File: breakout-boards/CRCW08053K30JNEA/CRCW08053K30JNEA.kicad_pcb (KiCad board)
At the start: 2 copper layers, 14 parts, among them J1 Conn_01x12, J2 Conn_01x12

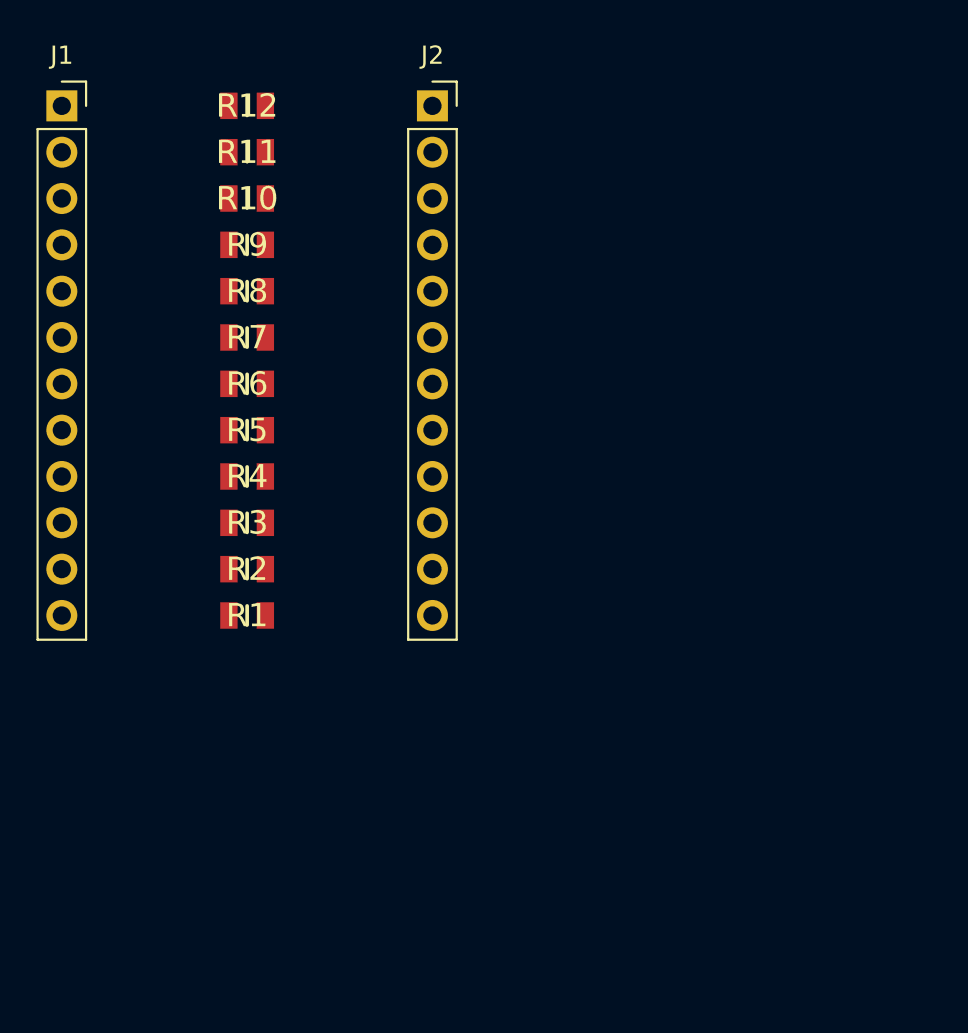
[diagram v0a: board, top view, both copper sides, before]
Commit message: feat: create footprints for resistor breakout boards
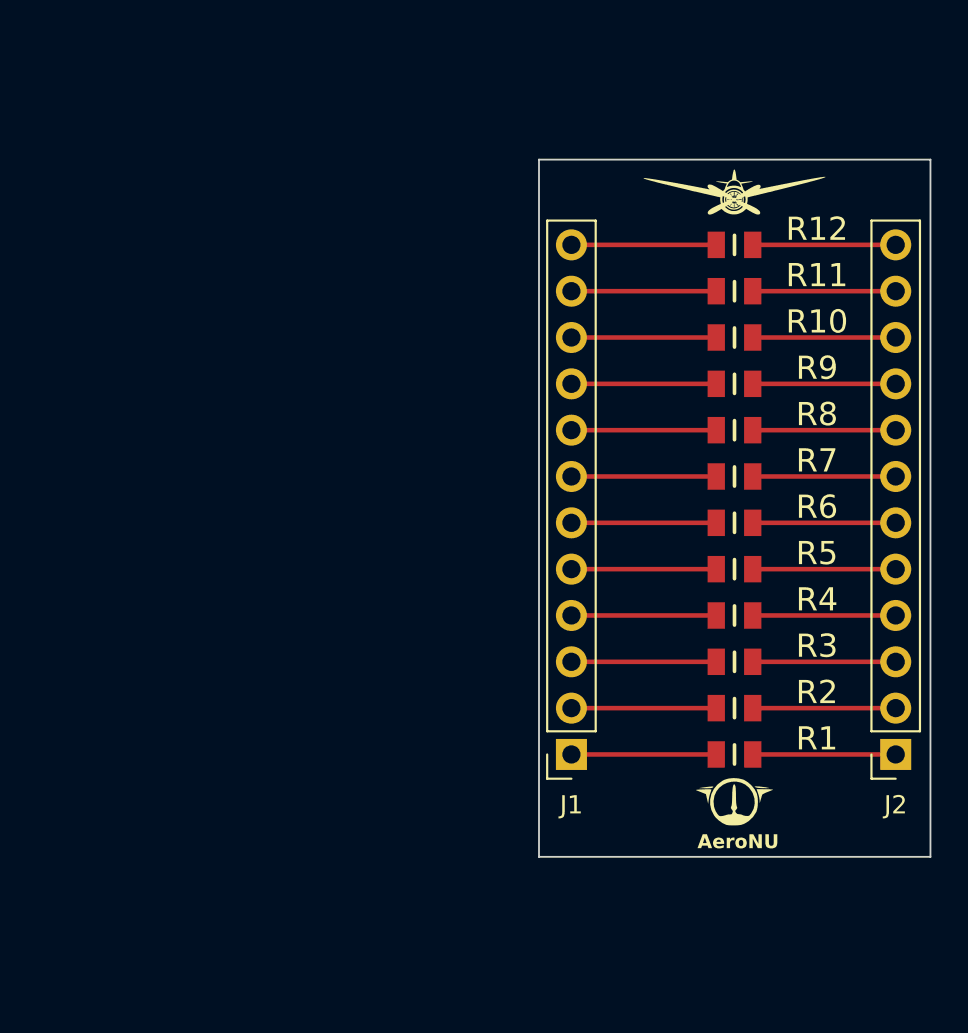
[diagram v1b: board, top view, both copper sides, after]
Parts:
- added AeroNU: LOGO, FixedWing:AeroNU - Logo (Smol), F.Cu at (174.2, 101.9)
- added FixedWing: LOGO, FixedWing:FixedWing - Logo (Smol), F.Cu at (174.1, 66.4)
- moved J1 45.2 mm to (165.1, 96.5), turned to 180 degrees
- moved J2 43.7 mm to (182.9, 96.5), turned to 180 degrees
- moved R1 27.8 mm to (174.0, 96.5)
- moved R10 27.8 mm to (174.0, 73.7)
- moved R11 27.8 mm to (174.0, 71.1)
- moved R12 27.8 mm to (174.0, 68.6)
- moved R2 27.8 mm to (174.0, 94.0)
- moved R3 27.8 mm to (174.0, 91.4)
- moved R4 27.8 mm to (174.0, 88.9)
- moved R5 27.8 mm to (174.0, 86.4)
- moved R6 27.8 mm to (174.0, 83.8)
- moved R7 27.8 mm to (174.0, 81.3)
- moved R8 27.8 mm to (174.0, 78.7)
- moved R9 27.8 mm to (174.0, 76.2)
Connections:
- R1 pad 1: Net-(J1-Pin_12) -> Net-(J1-Pin_1)
- R1 pad 2: Net-(J2-Pin_12) -> Net-(J2-Pin_1)
- R10 pad 1: Net-(J1-Pin_3) -> Net-(J1-Pin_10)
- R10 pad 2: Net-(J2-Pin_3) -> Net-(J2-Pin_10)
- R11 pad 1: Net-(J1-Pin_2) -> Net-(J1-Pin_11)
- R11 pad 2: Net-(J2-Pin_2) -> Net-(J2-Pin_11)
- R12 pad 1: Net-(J1-Pin_1) -> Net-(J1-Pin_12)
- R12 pad 2: Net-(J2-Pin_1) -> Net-(J2-Pin_12)
- R2 pad 1: Net-(J1-Pin_11) -> Net-(J1-Pin_2)
- R2 pad 2: Net-(J2-Pin_11) -> Net-(J2-Pin_2)
- R3 pad 1: Net-(J1-Pin_10) -> Net-(J1-Pin_3)
- R3 pad 2: Net-(J2-Pin_10) -> Net-(J2-Pin_3)
- R4 pad 1: Net-(J1-Pin_9) -> Net-(J1-Pin_4)
- R4 pad 2: Net-(J2-Pin_9) -> Net-(J2-Pin_4)
- R5 pad 1: Net-(J1-Pin_8) -> Net-(J1-Pin_5)
- R5 pad 2: Net-(J2-Pin_8) -> Net-(J2-Pin_5)
- R6 pad 1: Net-(J1-Pin_7) -> Net-(J1-Pin_6)
- R6 pad 2: Net-(J2-Pin_7) -> Net-(J2-Pin_6)
- R7 pad 1: Net-(J1-Pin_6) -> Net-(J1-Pin_7)
- R7 pad 2: Net-(J2-Pin_6) -> Net-(J2-Pin_7)
- R8 pad 1: Net-(J1-Pin_5) -> Net-(J1-Pin_8)
- R8 pad 2: Net-(J2-Pin_5) -> Net-(J2-Pin_8)
- R9 pad 1: Net-(J1-Pin_4) -> Net-(J1-Pin_9)
- R9 pad 2: Net-(J2-Pin_4) -> Net-(J2-Pin_9)
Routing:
- net Net-(J2-Pin_9): track 0.00 -> 7.94 mm
- net Net-(J2-Pin_8): track 0.00 -> 7.94 mm
- net Net-(J2-Pin_7): track 0.00 -> 7.94 mm
- net Net-(J2-Pin_6): track 0.00 -> 7.94 mm
- net Net-(J2-Pin_5): track 0.00 -> 7.94 mm
- net Net-(J2-Pin_4): track 0.00 -> 7.94 mm
- net Net-(J2-Pin_3): track 0.00 -> 7.94 mm
- net Net-(J2-Pin_2): track 0.00 -> 7.94 mm
- net Net-(J2-Pin_12): track 0.00 -> 7.94 mm
- net Net-(J2-Pin_11): track 0.00 -> 7.94 mm
- net Net-(J2-Pin_10): track 0.00 -> 7.94 mm
- net Net-(J2-Pin_1): track 0.00 -> 7.94 mm
- net Net-(J1-Pin_9): track 0.00 -> 7.84 mm
- net Net-(J1-Pin_8): track 0.00 -> 7.84 mm
- net Net-(J1-Pin_7): track 0.00 -> 7.84 mm
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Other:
- board outline added: 21.5 x 38.2 mm
- board text added: "AeroNU"
- board text added: "Designed By Ephram CJ and Matthew F"

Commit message: fix: change board alignement
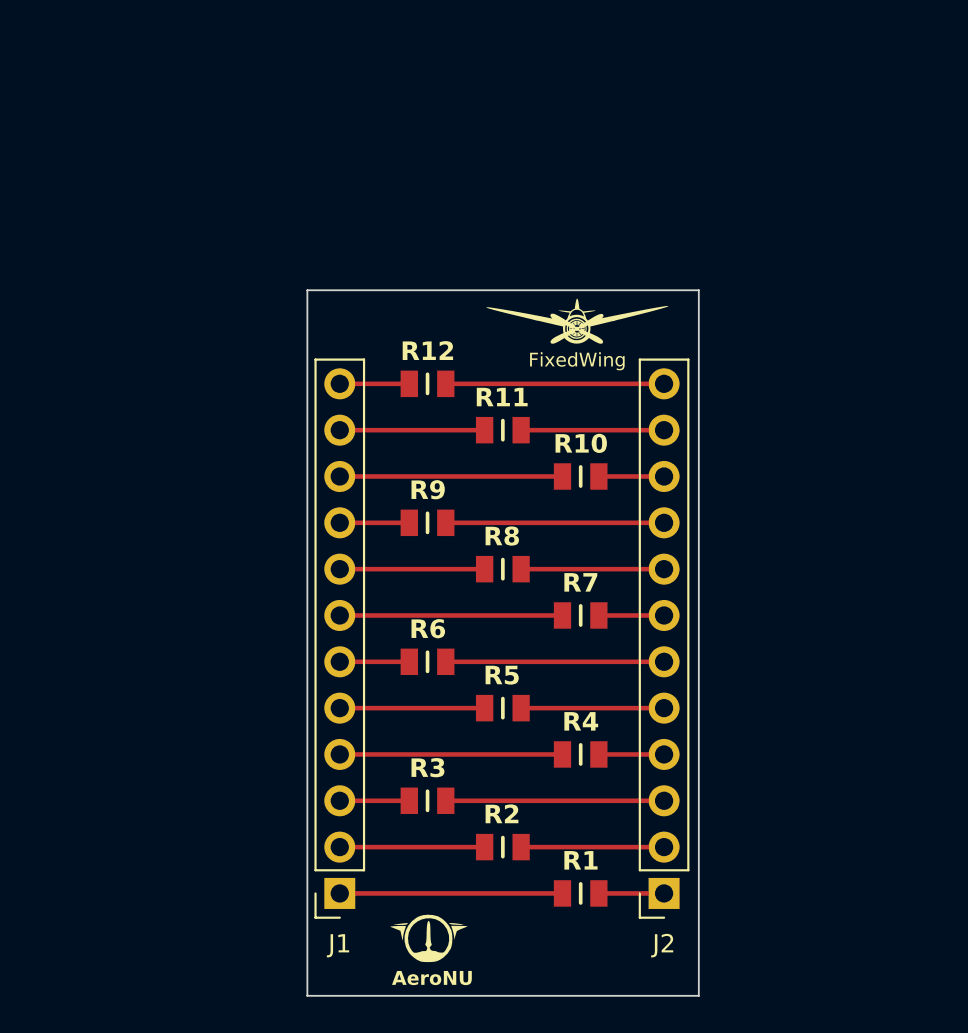
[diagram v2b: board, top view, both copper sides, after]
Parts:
- moved R12 18.5 mm to (157.2, 76.2)
- moved R3 18.5 mm to (157.2, 99.1)
- moved R6 18.5 mm to (157.2, 91.4)
- moved R9 18.5 mm to (157.2, 83.8)
- moved AeroNU 18.4 mm to (157.4, 109.4)
- moved J1 14.8 mm to (152.4, 104.1)
- moved J2 14.8 mm to (170.2, 104.1)
- moved R5 14.8 mm to (161.3, 94.0)
- moved R8 14.8 mm to (161.3, 86.4)
- moved R11 14.8 mm to (161.3, 78.7)
- moved R2 14.8 mm to (161.3, 101.6)
- moved R1 11.4 mm to (165.6, 104.1)
- moved R10 11.4 mm to (165.6, 81.3)
- moved R7 11.4 mm to (165.6, 88.9)
- moved R4 11.4 mm to (165.6, 96.5)
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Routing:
- net Net-(J1-Pin_7): track 7.84 -> 12.2 mm
- net Net-(J1-Pin_4): track 7.84 -> 12.2 mm
- net Net-(J1-Pin_10): track 7.84 -> 12.2 mm
- net Net-(J1-Pin_1): track 7.84 -> 12.2 mm
- net Net-(J2-Pin_7): track 7.94 -> 3.57 mm
- net Net-(J2-Pin_4): track 7.94 -> 3.57 mm
- net Net-(J2-Pin_10): track 7.94 -> 3.57 mm
- net Net-(J2-Pin_1): track 7.94 -> 3.57 mm
- net Net-(J2-Pin_9): track 7.94 -> 12.0 mm
- net Net-(J2-Pin_6): track 7.94 -> 12.0 mm
- net Net-(J2-Pin_3): track 7.94 -> 12.0 mm
- net Net-(J2-Pin_12): track 7.94 -> 12.0 mm
- net Net-(J1-Pin_9): track 7.84 -> 3.81 mm
- net Net-(J1-Pin_6): track 7.84 -> 3.81 mm
- net Net-(J1-Pin_3): track 7.84 -> 3.81 mm
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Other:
- board size 21.5 x 38.2 mm -> 21.5 x 38.7 mm

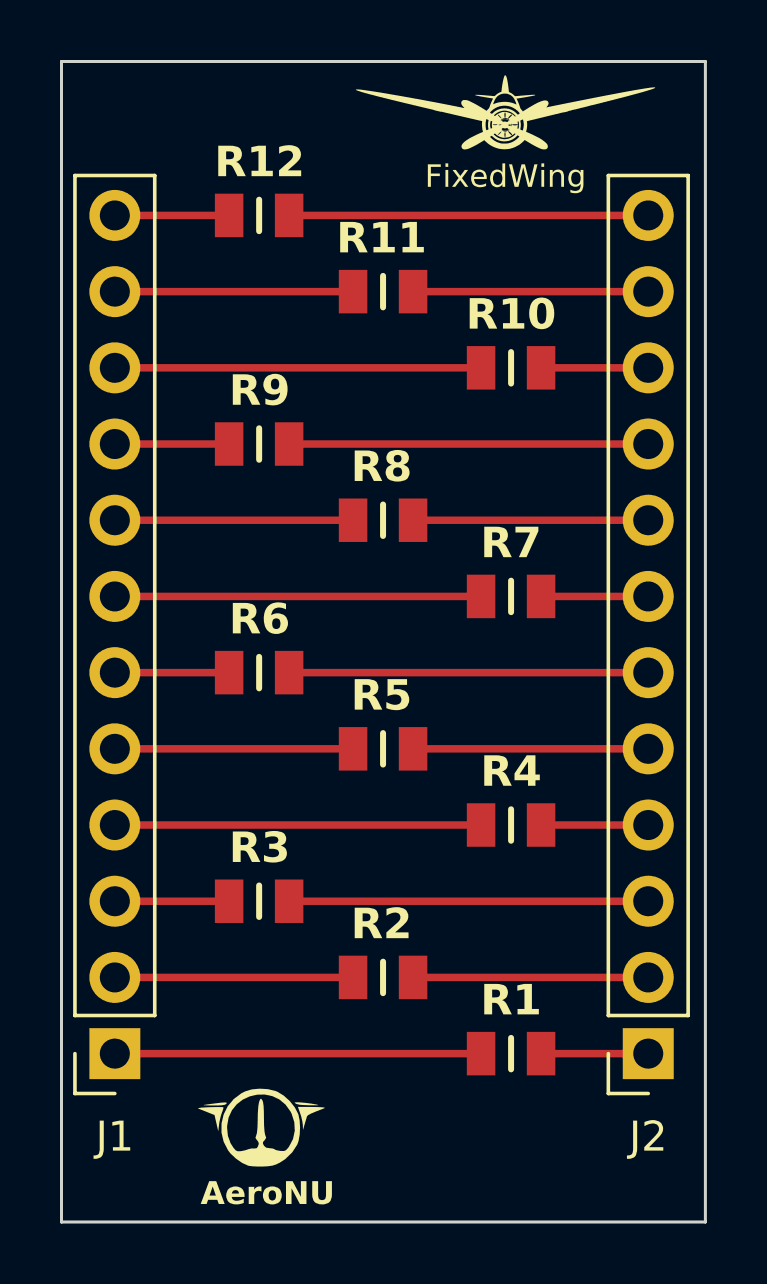
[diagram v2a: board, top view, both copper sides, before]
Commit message: feat: add fillets to all boards
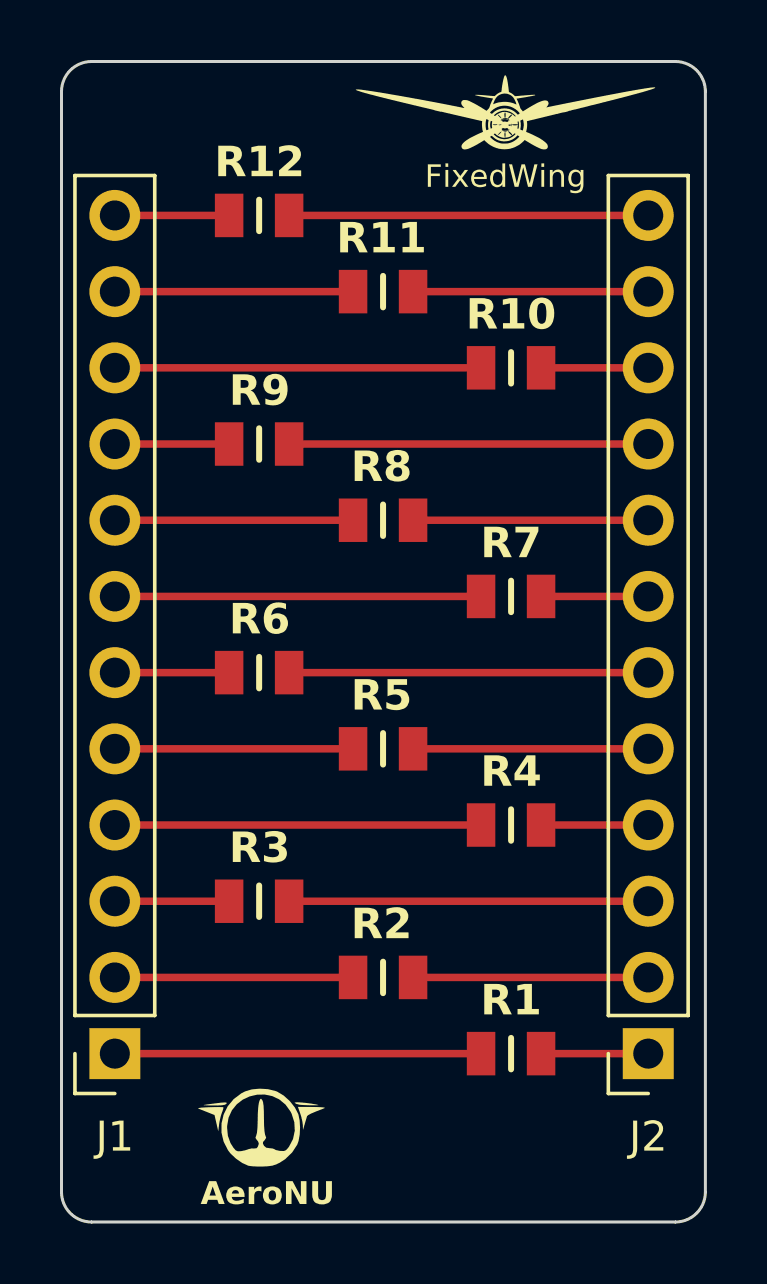
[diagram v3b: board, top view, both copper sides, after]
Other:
- outline, holes or cut-outs redrawn
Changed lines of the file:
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@@
       (outputformat 1)
       (mirror false)
-      (drillshape 1)
+      (drillshape 0)
       (scaleselection 1)
       (outputdirectory "")
@@
     )
   )
-  (gr_rect (start 150.622 71.0692) (end 172.085 109.7534)
-    (stroke (width 0.1) (type default)) (fill none) (layer "Edge.Cuts"))
+  (gr_line (start 150.622 108.7534) (end 150.622 72.0692)
+    (stroke (width 0.1) (type default)) (layer "Edge.Cuts"))
+  (gr_line (start 172.085 72.0692) (end 172.085 108.7534)
+    (stroke (width 0.1) (type default)) (layer "Edge.Cuts"))
+  (gr_arc (start 172.085 108.7534) (mid 171.792107 109.460507) (end 171.085 109.7534)
+    (stroke (width 0.1) (type default)) (layer "Edge.Cuts"))
+  (gr_line (start 151.622 71.0692) (end 171.085 71.0692)
+    (stroke (width 0.1) (type default)) (layer "Edge.Cuts"))
+  (gr_arc (start 151.622 109.7534) (mid 150.914893 109.460507) (end 150.622 108.7534)
+    (stroke (width 0.1) (type default)) (layer "Edge.Cuts"))
+  (gr_arc (start 150.622 72.0692) (mid 150.914893 71.362093) (end 151.622 71.0692)
+    (stroke (width 0.1) (type default)) (layer "Edge.Cuts"))
+  (gr_arc (start 171.085 71.0692) (mid 171.792107 71.362093) (end 172.085 72.0692)
+    (stroke (width 0.1) (type default)) (layer "Edge.Cuts"))
+  (gr_line (start 171.085 109.7534) (end 151.622 109.7534)
+    (stroke (width 0.1) (type default)) (layer "Edge.Cuts"))
   (gr_text "Designed By\nEphram CJ and Matthew F" (at 161.4424 108.6104) (layer "B.SilkS")
     (effects (font (size 0.762 0.762) (thickness 0.127) bold) (justify bottom mirror))
